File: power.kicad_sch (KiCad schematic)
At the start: 14 parts, among them U8 PLM62440APPQRJRTQ1

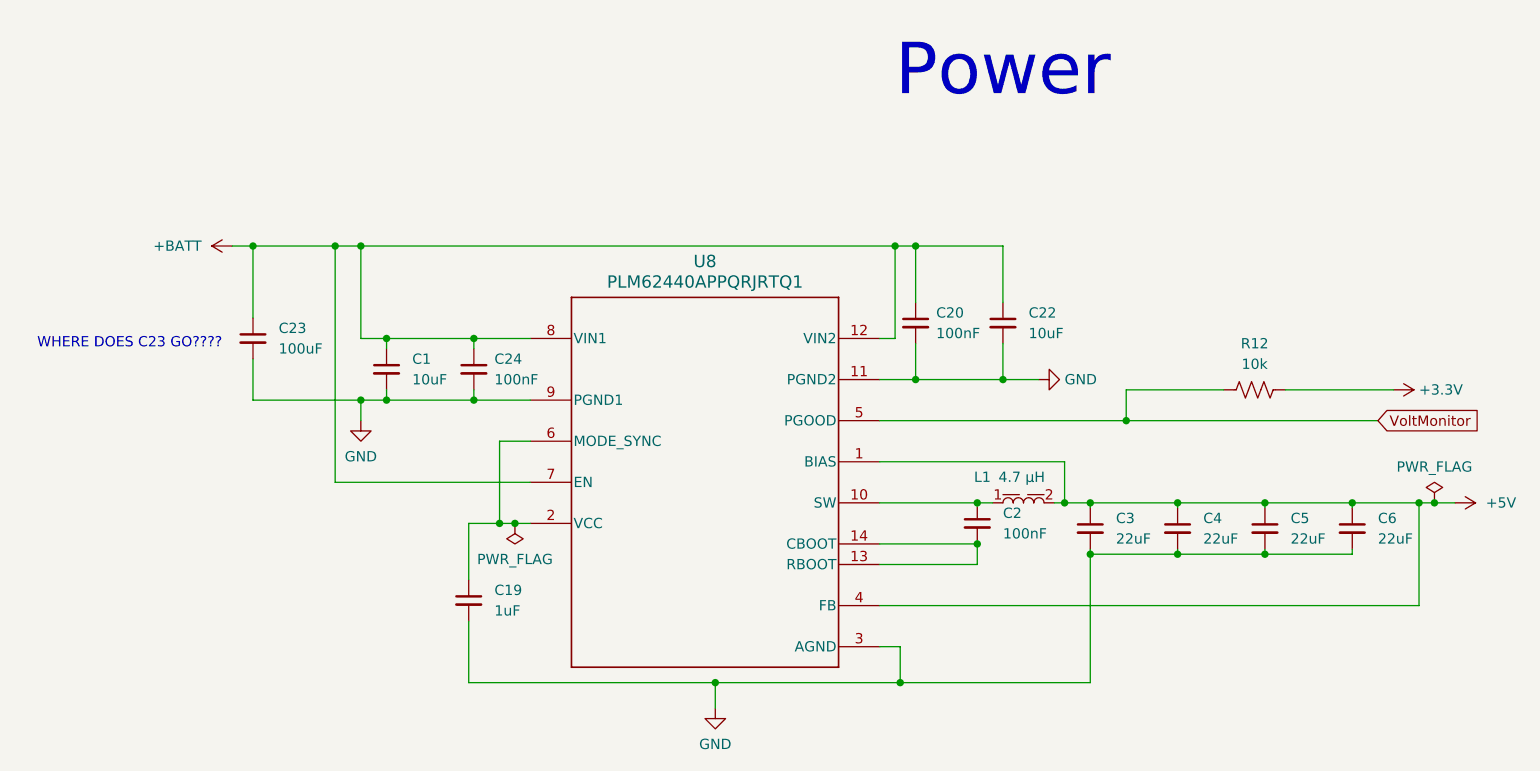
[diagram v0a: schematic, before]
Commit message: Fixed capacitor placement
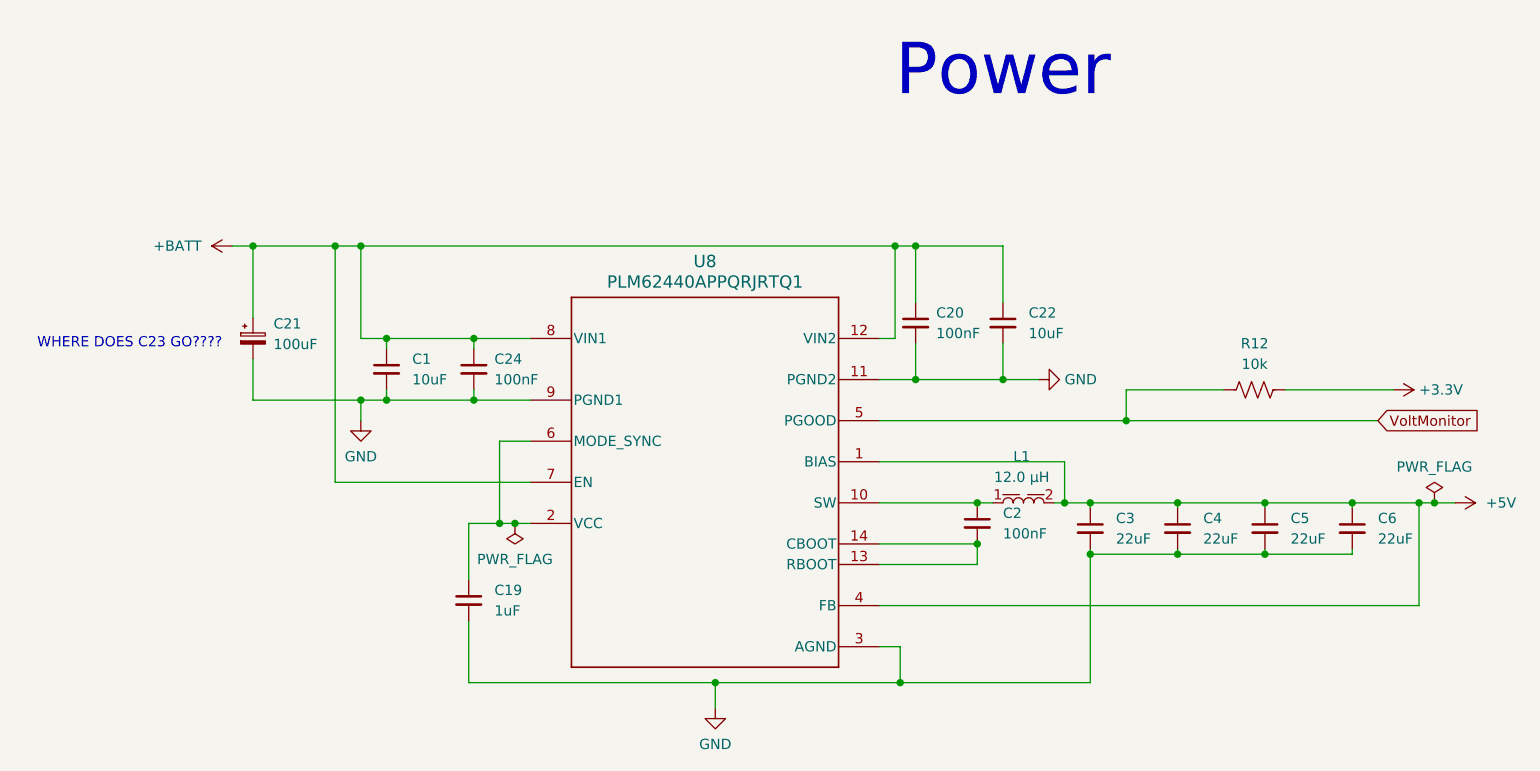
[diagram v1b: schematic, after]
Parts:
- removed C23: 100uF, Capacitor_SMD:C_0603_1608Metric, symbol Device:C_Small
- removed L1: 1090_78439369047, Inductor78439358047:L_Wurth_WE-XHMA-1090, symbol Inductor78439358047:1090_78439369047
- added C21: 100uF, Capacitor_SMD:CP_Elec_8x6.7, symbol Device:C_Polarized_Small
- added L1: 5030_7443845030120, BMP581:wurst7443845030120, symbol 7443845030120:5030_7443845030120
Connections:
- net +5V: now also L1.2
- net +BATT: now also C21.1
- net GND: now also C21.2
- net at C2.1, U8.10 (SW): now also L1.1

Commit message: Redid Footprints/Picked components
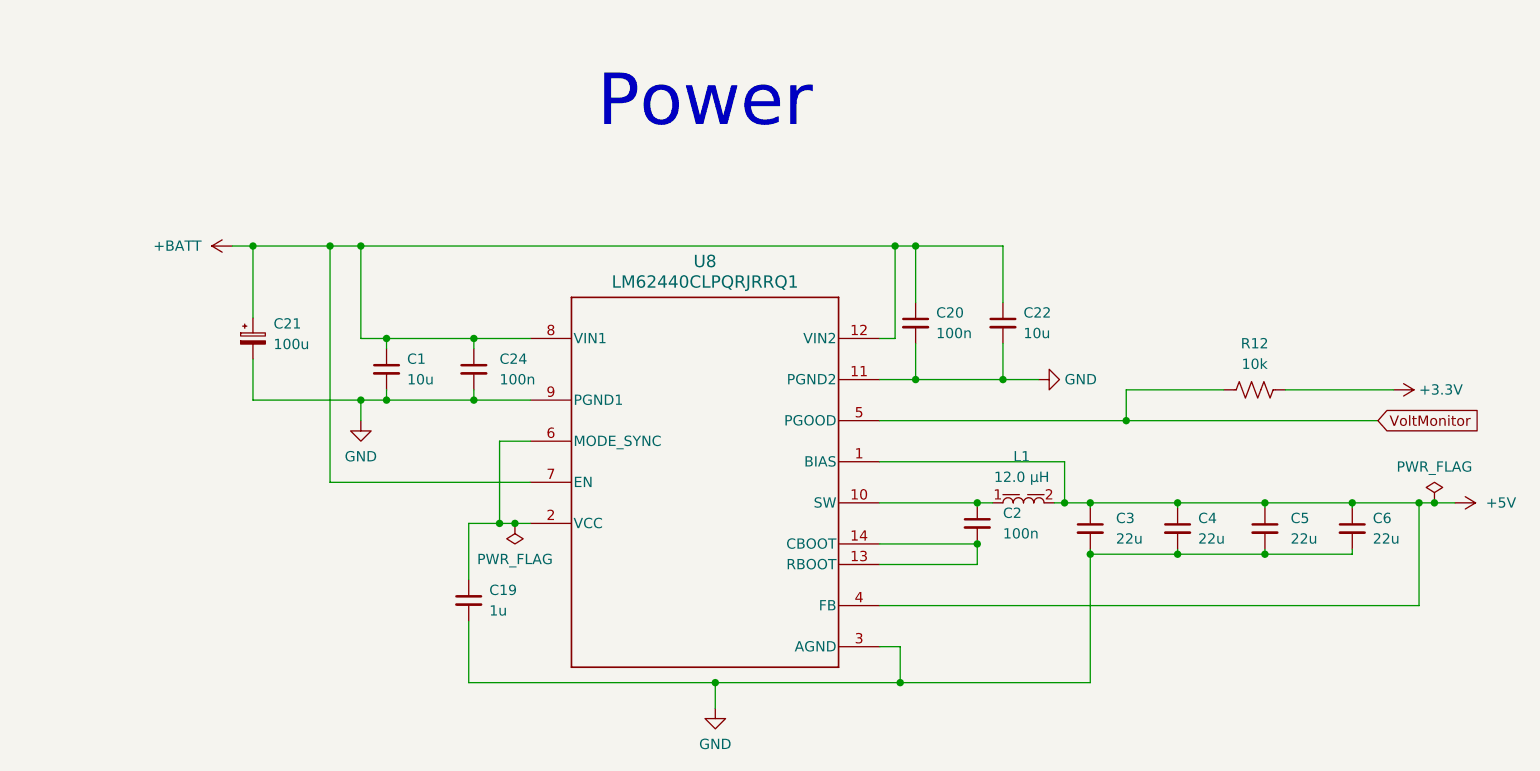
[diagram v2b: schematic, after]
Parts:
- C1, C22: value 10uF -> 10u; footprint Capacitor_SMD:C_0603_1608Metric -> Capacitor_SMD:C_0805_2012Metric
- C19: value 1uF -> 1u
- C2, C20, C24: value 100nF -> 100n
- C21: value 100uF -> 100u
- C3, C4, C5, C6: value 22uF -> 22u; footprint Capacitor_SMD:C_0603_1608Metric -> Capacitor_SMD:C_1206_3216Metric
- U8: value PLM62440APPQRJRTQ1 -> LM62440CLPQRJRRQ1
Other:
- note removed: "WHERE DOES C23 GO????"
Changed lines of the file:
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@@
 		(company "Notre Dame Rocketry Team")
-	)
-	(text "WHERE DOES C23 GO????"
-		(exclude_from_sim no)
-		(at 44.45 62.23 0)
-		(effects
-			(font
-				(size 1.27 1.27)
-			)
-		)
 	)
 	(text "Power"
 		(exclude_from_sim no)
-		(at 152.4 28.575 0)
+		(at 115.57 32.385 0)
 		(effects
 			(font
@@
 	)
 	(junction
-		(at 69.85 50.165)
-		(diameter 0)
-		(color 0 0 0 0)
-	)
-	(junction
 		(at 149.225 86.995)
 		(diameter 0)
@@
 	)
 	(junction
+		(at 69.215 50.165)
+		(diameter 0)
+		(color 0 0 0 0)
+	)
+	(junction
 		(at 195.58 81.915)
 		(diameter 0)
@@
 	(wire
 		(pts
-			(xy 69.85 50.165) (xy 69.85 79.375)
+			(xy 69.215 50.165) (xy 69.215 79.375)
 		)
 		(stroke
@@
 	(wire
 		(pts
+			(xy 69.215 50.165) (xy 73.025 50.165)
+		)
+		(stroke
+			(width 0)
+			(type default)
+		)
+	)
+	(wire
+		(pts
 			(xy 86.995 67.945) (xy 86.995 69.215)
 		)
@@
 	(wire
 		(pts
-			(xy 69.85 50.165) (xy 73.025 50.165)
-		)
-		(stroke
-			(width 0)
-			(type default)
-		)
-	)
-	(wire
-		(pts
 			(xy 137.16 71.755) (xy 167.64 71.755)
 		)
@@
 	(wire
 		(pts
-			(xy 93.98 79.375) (xy 69.85 79.375)
+			(xy 93.98 79.375) (xy 69.215 79.375)
 		)
 		(stroke
@@
 	(wire
 		(pts
-			(xy 59.69 50.165) (xy 69.85 50.165)
+			(xy 59.69 50.165) (xy 69.215 50.165)
 		)
 		(stroke
@@
 		(fields_autoplaced yes)
 		(property "Reference" "C4"
-			(at 177.165 83.8262 0)
-			(show_name no)
-			(do_not_autoplace no)
-			(effects
-				(font
-					(size 1.27 1.27)
-				)
-				(justify left)
-			)
-		)
-		(property "Value" "22uF"
-			(at 177.165 86.3662 0)
-			(show_name no)
-			(do_not_autoplace no)
-			(effects
-				(font
-					(size 1.27 1.27)
-				)
-				(justify left)
-			)
-		)
-		(property "Footprint" "Capacitor_SMD:C_0603_1608Metric"
+			(at 176.53 83.8262 0)
+			(show_name no)
+			(do_not_autoplace no)
+			(effects
+				(font
+					(size 1.27 1.27)
+				)
+				(justify left)
+			)
+		)
+		(property "Value" "22u"
+			(at 176.53 86.3662 0)
+			(show_name no)
+			(do_not_autoplace no)
+			(effects
+				(font
+					(size 1.27 1.27)
+				)
+				(justify left)
+			)
+		)
+		(property "Footprint" "Capacitor_SMD:C_1206_3216Metric"
 			(at 173.99 85.09 0)
 			(hide yes)
@@
 			)
 		)
-		(property "Value" "100uF"
+		(property "Value" "100u"
 			(at 62.23 62.3188 0)
 			(show_name no)
@@
 			)
 		)
-		(property "Datasheet" ""
+		(property "Datasheet" "A768KE107M1VLAS036"
 			(at 59.69 61.595 0)
 			(hide yes)
@@
 			)
 		)
-		(property "Value" "22uF"
+		(property "Value" "22u"
 			(at 166.37 86.3662 0)
 			(show_name no)
@@
 			)
 		)
-		(property "Footprint" "Capacitor_SMD:C_0603_1608Metric"
+		(property "Footprint" "Capacitor_SMD:C_1206_3216Metric"
 			(at 163.195 85.09 0)
 			(hide yes)
@@
 		(fields_autoplaced yes)
 		(property "Reference" "C19"
-			(at 89.535 92.7162 0)
-			(show_name no)
-			(do_not_autoplace no)
-			(effects
-				(font
-					(size 1.27 1.27)
-				)
-				(justify left)
-			)
-		)
-		(property "Value" "1uF"
-			(at 89.535 95.2562 0)
+			(at 88.9 92.7162 0)
+			(show_name no)
+			(do_not_autoplace no)
+			(effects
+				(font
+					(size 1.27 1.27)
+				)
+				(justify left)
+			)
+		)
+		(property "Value" "1u"
+			(at 88.9 95.2562 0)
 			(show_name no)
 			(do_not_autoplace no)
@@
 		(fields_autoplaced yes)
 		(property "Reference" "C24"
-			(at 89.535 64.1412 0)
-			(show_name no)
-			(do_not_autoplace no)
-			(effects
-				(font
-					(size 1.27 1.27)
-				)
-				(justify left)
-			)
-		)
-		(property "Value" "100nF"
-			(at 89.535 66.6812 0)
+			(at 90.17 64.1412 0)
+			(show_name no)
+			(do_not_autoplace no)
+			(effects
+				(font
+					(size 1.27 1.27)
+				)
+				(justify left)
+			)
+		)
+		(property "Value" "100n"
+			(at 90.17 66.6812 0)
 			(show_name no)
 			(do_not_autoplace no)
@@
 		(fields_autoplaced yes)
 		(property "Reference" "C22"
-			(at 155.575 58.4262 0)
-			(show_name no)
-			(do_not_autoplace no)
-			(effects
-				(font
-					(size 1.27 1.27)
-				)
-				(justify left)
-			)
-		)
-		(property "Value" "10uF"
-			(at 155.575 60.9662 0)
-			(show_name no)
-			(do_not_autoplace no)
-			(effects
-				(font
-					(size 1.27 1.27)
-				)
-				(justify left)
-			)
-		)
-		(property "Footprint" "Capacitor_SMD:C_0603_1608Metric"
+			(at 154.94 58.4262 0)
+			(show_name no)
+			(do_not_autoplace no)
+			(effects
+				(font
+					(size 1.27 1.27)
+				)
+				(justify left)
+			)
+		)
+		(property "Value" "10u"
+			(at 154.94 60.9662 0)
+			(show_name no)
+			(do_not_autoplace no)
+			(effects
+				(font
+					(size 1.27 1.27)
+				)
+				(justify left)
+			)
+		)
+		(property "Footprint" "Capacitor_SMD:C_0805_2012Metric"
 			(at 152.4 59.69 0)
 			(hide yes)
@@
 			)
 		)
-		(property "Value" "PLM62440APPQRJRTQ1"
+		(property "Value" "LM62440CLPQRJRRQ1"
 			(at 115.57 54.61 0)
 			(show_name no)
@@
 			)
 		)
-		(property "Value" "22uF"
+		(property "Value" "22u"
 			(at 187.96 86.3662 0)
 			(show_name no)
@@
 			)
 		)
-		(property "Footprint" "Capacitor_SMD:C_0603_1608Metric"
+		(property "Footprint" "Capacitor_SMD:C_1206_3216Metric"
 			(at 184.785 85.09 0)
 			(hide yes)
@@
 		(in_pos_files yes)
 		(dnp no)
-		(fields_autoplaced yes)
 		(property "Reference" "C20"
 			(at 144.145 58.4262 0)
@@
 			)
 		)
-		(property "Value" "100nF"
+		(property "Value" "100n"
 			(at 144.145 60.9662 0)
 			(show_name no)
@@
 		(fields_autoplaced yes)
 		(property "Reference" "C1"
-			(at 79.375 64.1412 0)
-			(show_name no)
-			(do_not_autoplace no)
-			(effects
-				(font
-					(size 1.27 1.27)
-				)
-				(justify left)
-			)
-		)
-		(property "Value" "10uF"
-			(at 79.375 66.6812 0)
-			(show_name no)
-			(do_not_autoplace no)
-			(effects
-				(font
-					(size 1.27 1.27)
-				)
-				(justify left)
-			)
-		)
-		(property "Footprint" "Capacitor_SMD:C_0603_1608Metric"
+			(at 78.74 64.1412 0)
+			(show_name no)
+			(do_not_autoplace no)
+			(effects
+				(font
+					(size 1.27 1.27)
+				)
+				(justify left)
+			)
+		)
+		(property "Value" "10u"
+			(at 78.74 66.6812 0)
+			(show_name no)
+			(do_not_autoplace no)
+			(effects
+				(font
+					(size 1.27 1.27)
+				)
+				(justify left)
+			)
+		)
+		(property "Footprint" "Capacitor_SMD:C_0805_2012Metric"
 			(at 76.2 65.405 0)
 			(hide yes)
@@
 		(fields_autoplaced yes)
 		(property "Reference" "C6"
-			(at 198.755 83.8262 0)
-			(show_name no)
-			(do_not_autoplace no)
-			(effects
-				(font
-					(size 1.27 1.27)
-				)
-				(justify left)
-			)
-		)
-		(property "Value" "22uF"
-			(at 198.755 86.3662 0)
-			(show_name no)
-			(do_not_autoplace no)
-			(effects
-				(font
-					(size 1.27 1.27)
-				)
-				(justify left)
-			)
-		)
-		(property "Footprint" "Capacitor_SMD:C_0603_1608Metric"
+			(at 198.12 83.8262 0)
+			(show_name no)
+			(do_not_autoplace no)
+			(effects
+				(font
+					(size 1.27 1.27)
+				)
+				(justify left)
+			)
+		)
+		(property "Value" "22u"
+			(at 198.12 86.3662 0)
+			(show_name no)
+			(do_not_autoplace no)
+			(effects
+				(font
+					(size 1.27 1.27)
+				)
+				(justify left)
+			)
+		)
+		(property "Footprint" "Capacitor_SMD:C_1206_3216Metric"
 			(at 195.58 85.09 0)
 			(hide yes)
@@
 			)
 		)
-		(property "Value" "100nF"
+		(property "Value" "100n"
 			(at 152.4 85.7312 0)
 			(show_name no)

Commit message: finalized
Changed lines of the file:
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@@
-	)
-	(junction
-		(at 205.74 81.915)
-		(diameter 0)
-		(color 0 0 0 0)
 	)
 	(junction
@@
 	(wire
 		(pts
-			(xy 203.835 81.915) (xy 205.74 81.915)
+			(xy 203.835 81.915) (xy 208.28 81.915)
 		)
 		(stroke
@@
 		(pts
 			(xy 86.995 69.215) (xy 93.98 69.215)
-		)
-		(stroke
-			(width 0)
-			(type default)
-		)
-	)
-	(wire
-		(pts
-			(xy 205.74 81.915) (xy 208.28 81.915)
 		)
 		(stroke
@@
 					(unit 1)
 				)
-			)
-		)
-	)
-	(symbol
-		(lib_id "power:PWR_FLAG")
-		(at 205.74 81.915 0)
-		(unit 1)
-		(body_style 1)
-		(exclude_from_sim no)
-		(in_bom yes)
-		(on_board yes)
-		(in_pos_files yes)
-		(dnp no)
-		(fields_autoplaced yes)
-		(property "Reference" "#FLG011"
-			(at 205.74 80.01 0)
-			(hide yes)
-			(show_name no)
-			(do_not_autoplace no)
-			(effects
-				(font
-					(size 1.27 1.27)
-				)
-			)
-		)
-		(property "Value" "PWR_FLAG"
-			(at 205.74 77.47 0)
-			(show_name no)
-			(do_not_autoplace no)
-			(effects
-				(font
-					(size 1.27 1.27)
-				)
-			)
-		)
-		(property "Footprint" ""
-			(at 205.74 81.915 0)
-			(hide yes)
-			(show_name no)
-			(do_not_autoplace no)
-			(effects
-				(font
-					(size 1.27 1.27)
-				)
-			)
-		)
-		(property "Datasheet" ""
-			(at 205.74 81.915 0)
-			(hide yes)
-			(show_name no)
-			(do_not_autoplace no)
-			(effects
-				(font
-					(size 1.27 1.27)
-				)
-			)
-		)
-		(property "Description" "Special symbol for telling ERC where power comes from"
-			(at 205.74 81.915 0)
-			(hide yes)
-			(show_name no)
-			(do_not_autoplace no)
-			(effects
-				(font
-					(size 1.27 1.27)
-				)
-			)
-		)
-		(pin "1"
-		)
-		(instances
-			(project "ACS PCB"
-				(path "/67a598cb-afc0-4277-b58a-8f35d31efc48/8f3a2ae2-24ee-4ca8-930f-6202803bc7c8"
-					(reference "#FLG011")
-					(unit 1)
-				)
